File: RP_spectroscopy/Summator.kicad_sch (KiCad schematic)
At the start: 32 parts, among them U1 AD8603, U2 ADG417BR, U3 AD8397

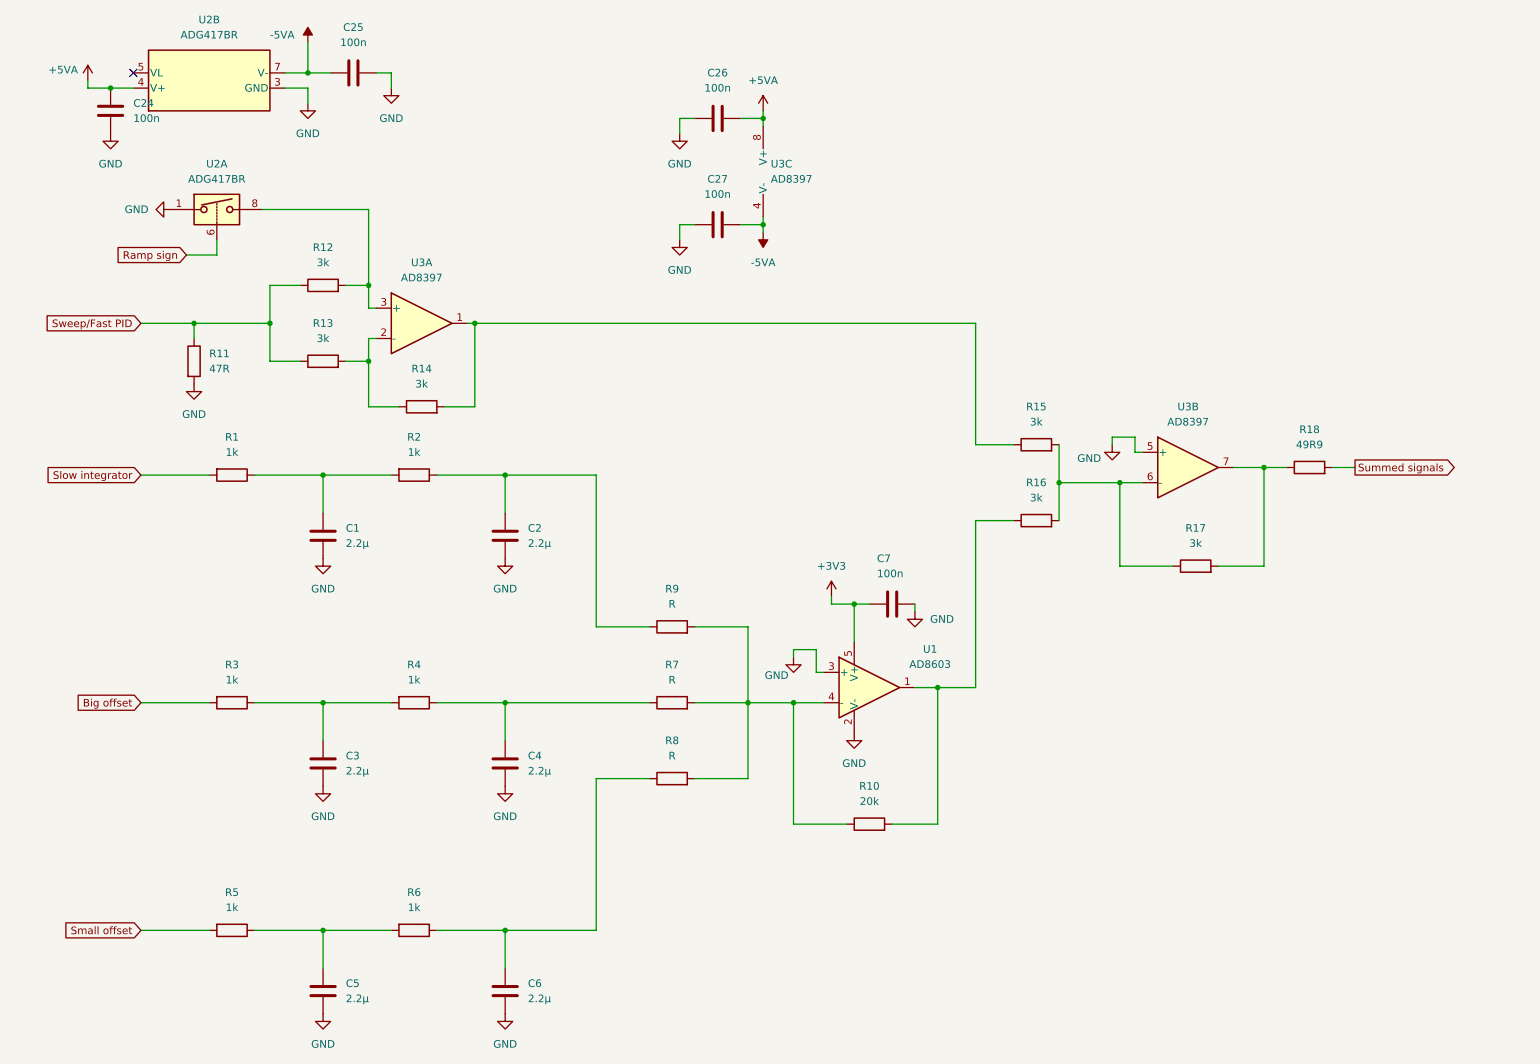
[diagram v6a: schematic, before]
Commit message: Check of the availability of all the components and of the footprints. Added the demultiplexer part of the circuit. Some graphical changes. Changed the values of some R in order to match the ones available in the officina elettronica.
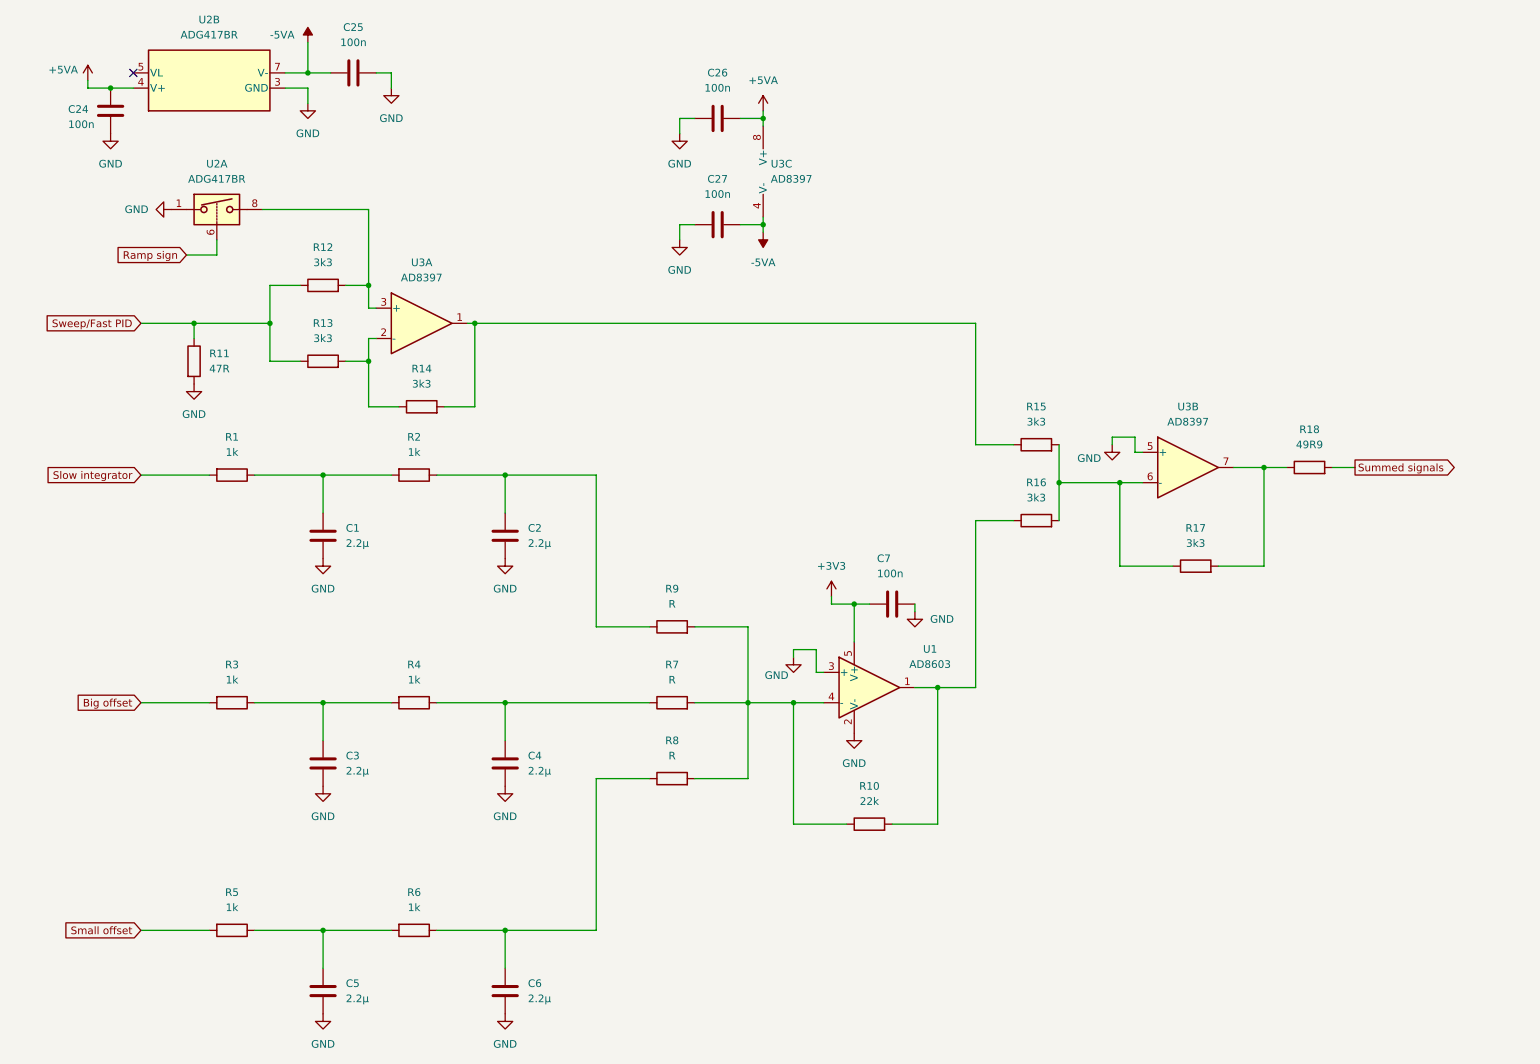
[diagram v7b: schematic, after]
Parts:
- R10: value 20k -> 22k
- R12, R13, R14, R15, R16, R17: value 3k -> 3k3
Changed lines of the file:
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@@
 	)
 	(junction
-		(at 33.02 27.94)
-		(diameter 0)
-		(color 0 0 0 0)
-	)
-	(junction
 		(at 171.45 128.27)
 		(diameter 0)
@@
 		(color 0 0 0 0)
 	)
+	(junction
+		(at 33.02 27.94)
+		(diameter 0)
+		(color 0 0 0 0)
+	)
 	(no_connect
 		(at 36.83 25.4)
@@
 	(wire
 		(pts
-			(xy 33.02 27.94) (xy 36.83 27.94)
-		)
-		(stroke
-			(width 0)
-			(type default)
-		)
-	)
-	(wire
-		(pts
 			(xy 29.21 27.94) (xy 33.02 27.94)
 		)
@@
 		)
 	)
+	(wire
+		(pts
+			(xy 33.02 27.94) (xy 36.83 27.94)
+		)
+		(stroke
+			(width 0)
+			(type default)
+		)
+	)
 	(global_label "Big offset"
 		(shape input)
@@
 			)
 		)
-		(property "Value" "3k"
+		(property "Value" "3k3"
 			(at 68.58 69.85 90)
 			(effects
@@
 			)
 		)
-		(property "Value" "3k"
+		(property "Value" "3k3"
 			(at 85.09 77.47 90)
 			(effects
@@
 			)
 		)
-		(property "Value" "20k"
+		(property "Value" "22k"
 			(at 160.02 147.32 90)
 			(effects
@@
 			)
 		)
-		(property "Value" "3k"
+		(property "Value" "3k3"
 			(at 68.58 57.15 90)
 			(effects
@@
 			)
 		)
-		(property "Value" "3k"
+		(property "Value" "3k3"
 			(at 187.96 96.52 90)
 			(effects
@@
 			)
 		)
-		(property "Value" "3k"
+		(property "Value" "3k3"
 			(at 214.63 104.14 90)
 			(effects
@@
 		(on_board yes)
 		(dnp no)
-		(fields_autoplaced yes)
 		(property "Reference" "C24"
-			(at 36.83 30.4799 0)
+			(at 25.908 31.496 0)
 			(effects
 				(font
@@
 		)
 		(property "Value" "100n"
-			(at 36.83 33.0199 0)
+			(at 25.908 34.0361 0)
 			(effects
 				(font
@@
 			)
 		)
-		(property "Value" "3k"
+		(property "Value" "3k3"
 			(at 187.96 83.82 90)
 			(effects

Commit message: Added the summator parameters. Started to do the wireings
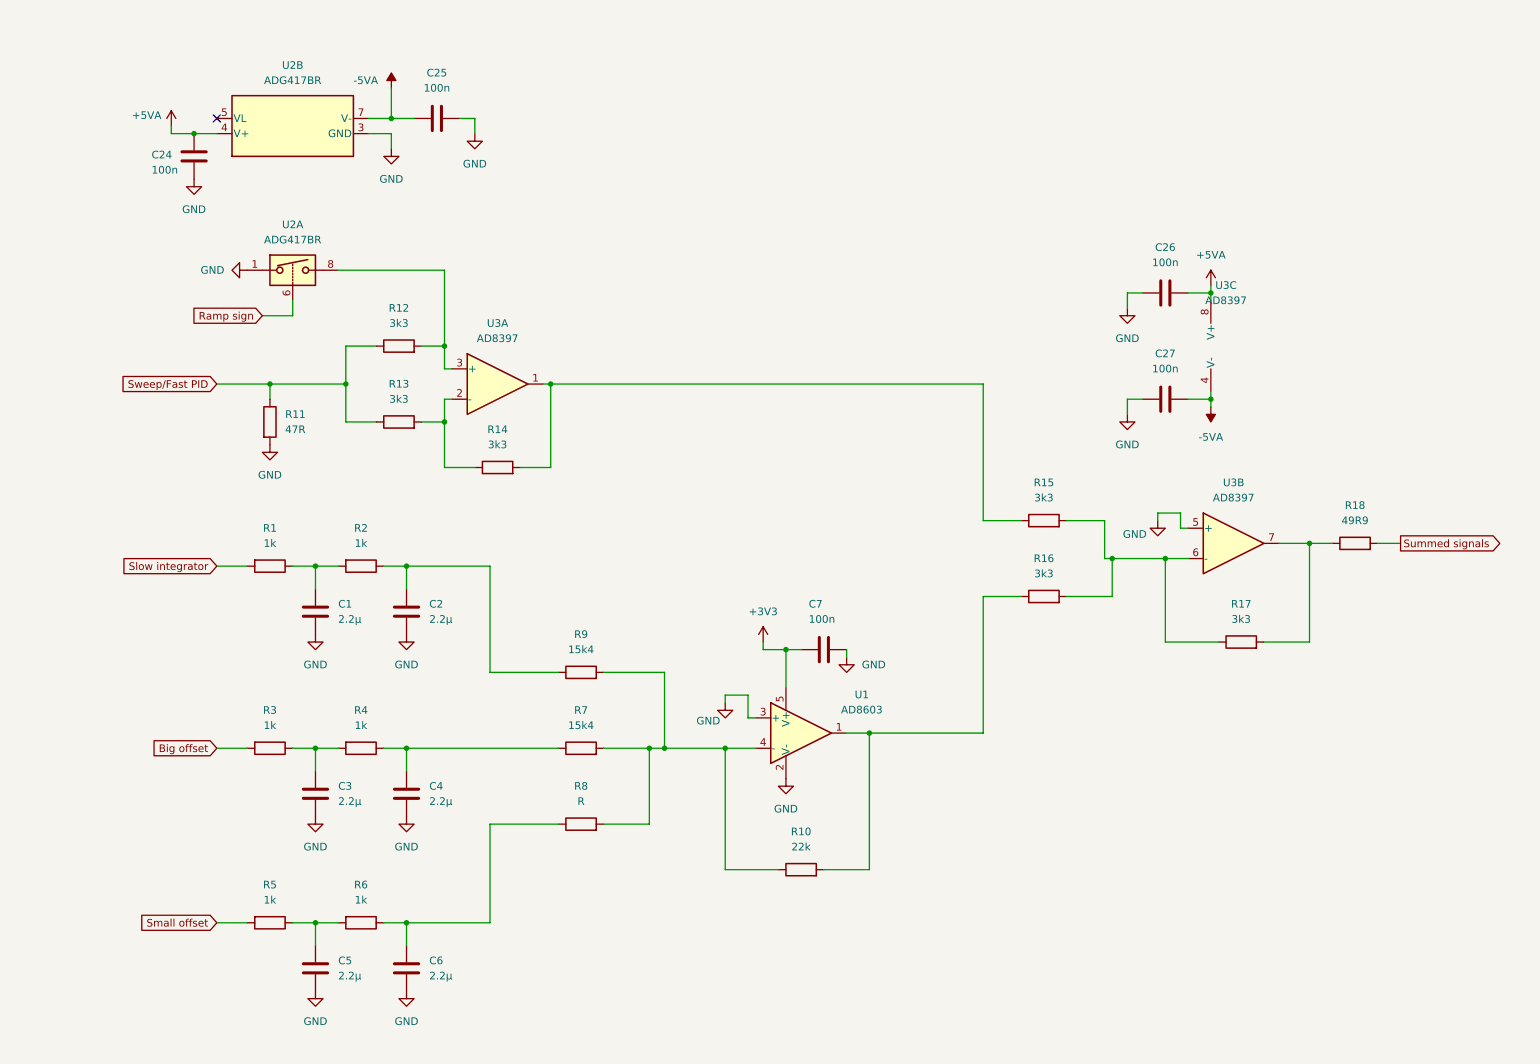
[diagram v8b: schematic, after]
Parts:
- R7, R9: value R -> 15k4
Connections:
- net -5VA: no longer U3.9 (V-)
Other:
- moved on the sheet: C1, C2, C24, C25, C26, C27, C3, C4, C5, C6, C7, R1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
